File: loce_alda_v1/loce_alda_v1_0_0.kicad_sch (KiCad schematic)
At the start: 82 parts, among them J2 battery_conn_r, J3 track_point_left, J4 niceview_left, J5 niceview_right, J6 track_point_right, SW1 SW_Push, SW10 SW_Push, SW10_r1 SW_Push, SW11 SW_Push, SW11_r1 SW_Push, SW12 SW_Push, SW12_r1 SW_Push, SW13 SW_Push, SW13_r1 SW_Push, SW14 SW_Push, SW14_r1 SW_Push, SW15 SW_Push, SW15_r1 SW_Push, SW16 SW_Push, SW16_r1 SW_Push, SW17 SW_Push, SW17_r1 SW_Push, SW1_r1 SW_Push, SW2 SW_Push, SW2_r1 SW_Push, SW3 SW_Push, SW3_r1 SW_Push, SW4 SW_Push, SW4_r1 SW_Push, SW5 SW_Push, SW5_r1 SW_Push, SW6 SW_Push, SW6_r1 SW_Push, SW7 SW_Push, SW7_r1 SW_Push, SW8 SW_Push, SW8_r1 SW_Push, SW9 SW_Push, SW9_r1 SW_Push, U1 ProMicro-kbd, U2 ProMicro-kbd

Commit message: feat: basic shematics
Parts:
- removed BT1: 1044, 1044:BAT_1044, symbol 1044:1044
- removed Bat+r1, BatGNDr1: MountingHole_Pad, kbd:1pin_conn, symbol Mechanical:MountingHole_Pad
- removed J2: battery_conn_r, Connector_JST:JST_PH_S2B-PH-K_1x02_P2.00mm_Horizontal, symbol Connector:Conn_01x02_Female
- removed U1, U2: ProMicro-kbd, Arduino:Sparkfun_Pro_Micro, symbol Arduino:Sparkfun_Pro_Micro
- added BT1, BT3: Battery, keystone82:batteryHolder_10440_Keystone_82, symbol Device:Battery
- added D35, D36: 1N4148W, Diode_SMD:D_SOD-123, symbol Diode:1N4148W
- added J1, J10, J2, J8: batt_conn, Connector_PinHeader_2.54mm:PinHeader_1x02_P2.54mm_Vertical, symbol Connector:Conn_01x02_Pin
- added J11, J12, J7, J9: batt_conn, Connector_PinSocket_2.54mm:PinSocket_1x02_P2.54mm_Vertical, symbol Connector:Conn_01x02_Socket
- added J13, J14: nfc, Connector_PinSocket_2.54mm:PinSocket_1x02_P2.54mm_Vertical, symbol Connector:Conn_01x02_Socket
- added J15, J16: extra_btn, Connector_PinSocket_2.54mm:PinSocket_1x02_P2.54mm_Vertical, symbol Connector:Conn_01x02_Socket
- added J17: TP_thumb_r, trackpoint:trackpoint_mount_t460s_offset, symbol Connector:Conn_01x01_Pin
- added J18: TP_thumb, trackpoint:trackpoint_mount_t460s_offset, symbol Connector:Conn_01x01_Pin
- added J19: TP_index_r, trackpoint:trackpoint_mount_t460s_offset, symbol Connector:Conn_01x01_Pin
- added J20: TP_index, trackpoint:trackpoint_mount_t460s_offset, symbol Connector:Conn_01x01_Pin
- added U1, U2: SeeeduinoXIAO_BLE, xiao:XIAO-nRF52840-SMD, symbol XIAO:SeeeduinoXIAO_BLE
- added U3, U4: 74HC595, sn74hc595dr:D0016A_N, symbol 74xx:74HC595
- SW1, SW10, SW10_r1, SW11, SW11_r1, SW12, SW12_r1, SW13, SW13_r1, SW14, SW14_r1, SW15, SW15_r1, SW16, SW16_r1, SW17, SW17_r1, SW1_r1, SW2, SW2_r1, SW3, SW3_r1, SW4, SW4_r1, SW5, SW5_r1, SW6, SW6_r1, SW7, SW7_r1, SW8, SW8_r1, SW9, SW9_r1: footprint choc_switch_3d:SW_Hotswap_Kailh_Choc_V1_tweaked -> choc_switch:SW_Hotswap_Kailh_Choc_V1_tweaked_no_clickbar
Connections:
- net ROW3 is gone; now on net ROW2: D16.1 (K), D17.1 (K)
- net ROW3_r is gone; now on net ROW2_r: D33.1 (K), D34.1 (K)
- net BT+: now also BT3.1 (+), J10.1 (Pin_1), J10.2 (Pin_2), J12.1 (Pin_1), J12.2 (Pin_2), J8.1 (Pin_1), J8.2 (Pin_2), J9.1 (Pin_1), J9.2 (Pin_2)
- net BT+_r: now also BT1.1 (+)
- net COL0: now also SW13.1, SW7.1, U4.1 (QB); no longer SW11.1, SW6.1
- net COL0_r: now also SW13_r1.1, SW1_r1.1, SW7_r1.1, U3.1 (QB); no longer SW10_r1.1, SW15_r1.1, SW17_r1.1, SW5_r1.1
- net COL1: now also SW14.1, SW8.1, U4.2 (QC); no longer SW12.1, SW7.1
- net COL1_r: now also SW2_r1.1, SW8_r1.1, U3.2 (QC); no longer SW16_r1.1, SW4_r1.1, SW9_r1.1
- net COL2: now also SW15.1, SW9.1, U4.15 (QA); no longer SW13.1, SW8.1
- net COL2_r: now also SW15_r1.1, SW9_r1.1, U3.15 (QA); no longer SW13_r1.1, SW8_r1.1
- net COL3: now also SW10.1, U4.3 (QD); no longer SW14.1, SW9.1
- net COL3_r: now also SW10_r1.1, SW16_r1.1, SW4_r1.1, U3.3 (QD); no longer SW12_r1.1, SW2_r1.1, SW7_r1.1
- net COL4: now also SW11.1, U4.5 (QF); no longer SW10.1, SW15.1
- net COL4_r: now also SW17_r1.1, SW5_r1.1, U3.5 (QF); no longer SW1_r1.1, SW6_r1.1
- net CS: now also U1.2 (PA4_A1_D1)
- net CS_r: now also U2.2 (PA4_A1_D1)
- net IPD_CLK: now also J3.5 (Pin_5), U1.6 (PA9_A5_D5_SCL)
- net IPD_CLK_r: now also J6.5 (Pin_5), U2.6 (PA9_A5_D5_SCL)
- net IPD_DATA: now also J3.11 (Pin_11), U1.5 (PA8_A4_D4_SDA)
- net IPD_DATA_r: now also J6.11 (Pin_11), U2.5 (PA8_A4_D4_SDA)
- net IPD_RST: now also J3.10 (Pin_10), U1.7 (PB08_A6_D6_TX)
- net IPD_RST_r: now also J6.10 (Pin_10), U2.7 (PB08_A6_D6_TX)
- net MISO: now also U1.11 (PA6_A10_D10_MOSI)
- net MISO_r: now also U2.10 (PA5_A9_D9_MISO)
- net MOSI: now also U1.10 (PA5_A9_D9_MISO), U4.14 (SER)
- net MOSI_r: now also U2.11 (PA6_A10_D10_MOSI), U3.14 (SER)
- net ROW0: now also D6.1 (K), U1.1 (PA02_A0_D0)
- net ROW0_r: now also D23.1 (K), U2.1 (PA02_A0_D0)
- net ROW1: now also D11.1 (K), D12.1 (K), U1.3 (PA10_A2_D2); no longer D6.1 (K)
- net ROW1_r: now also D28.1 (K), D29.1 (K), U2.3 (PA10_A2_D2); no longer D23.1 (K)
- net ROW2: now also D36.1 (K), U1.4 (PA11_A3_D3); no longer D11.1 (K), D12.1 (K)
- net ROW2_r: now also D35.1 (K), U2.4 (PA11_A3_D3); no longer D28.1 (K), D29.1 (K)
- net SCK: now also U1.9 (PA7_A8_D8_SCK), U4.11 (SRCLK)
- net SCK_r: now also U2.9 (PA7_A8_D8_SCK), U3.11 (SRCLK)
- net gnd: now also J3.6 (Pin_6), BT3.2 (-), J1.1 (Pin_1), J1.2 (Pin_2), J11.1 (Pin_1), J11.2 (Pin_2), J2.1 (Pin_1), J2.2 (Pin_2), J7.1 (Pin_1), J7.2 (Pin_2), U1.13 (GND), U4.13 (~{OE}), U4.8 (GND)
- net gnd_r: now also J6.6 (Pin_6), BT1.2 (-), U2.13 (GND), U3.13 (~{OE}), U3.8 (GND)
- net raw: now also U1.16 (BAT+)
- net reset: now also U1.15 (RESET)
- net reset_r: now also U2.15 (RESET)
- net vcc: now also J3.12 (Pin_12), U1.12 (3V3)
- net vcc_r: now also J6.12 (Pin_12), U2.12 (3V3)
- net at D32.2 (A): now also SW15_r1.2; no longer SW11_r1.2
- net at SW16_r1.2: now also D33.2 (A); no longer D34.2 (A)
- net at D23.2 (A): now also SW6_r1.2; no longer SW10_r1.2
- net at SW5_r1.2: now also D22.2 (A); no longer D18.2 (A)
- net at SW7_r1.2: now also D24.2 (A); no longer D26.2 (A)
- net at D19.2 (A): now also SW2_r1.2; no longer SW4_r1.2
- net at D28.2 (A): now also SW11_r1.2; no longer SW15_r1.2
- net at SW12_r1.2: now also D29.2 (A); no longer D31.2 (A)
- net at SW17_r1.2: now also D34.2 (A); no longer D33.2 (A)
- net at SW14_r1.2: now also D31.2 (A); no longer D29.2 (A)
- net at SW1_r1.2: now also D18.2 (A); no longer D22.2 (A)
- net at SW9_r1.2: now also D26.2 (A); no longer D24.2 (A)
- net at D21.2 (A): now also SW4_r1.2; no longer SW2_r1.2
- net at D27.2 (A): now also SW10_r1.2; no longer SW6_r1.2
- new net: D36.2 (A), J15.2 (Pin_2)
- new net: D35.2 (A), J16.2 (Pin_2)
- new net: J13.1 (Pin_1), U1.18 (J13-pin_1)
- new net: J13.2 (Pin_2), U1.17 (J13-pin_2)
- new net: U3.10 (~{SRCLR}), U3.16 (VCC)
- new net: U4.10 (~{SRCLR}), U4.16 (VCC)
- new net COL5: J15.1 (Pin_1), SW12.1, SW6.1, U4.4 (QE)
- new net COL5_r: J16.1 (Pin_1), SW12_r1.1, SW6_r1.1, U3.4 (QE)
- new net SR_CS: U1.8 (PB09_A7_D7_RX), U4.12 (RCLK)
- new net SR_CS_r: U2.8 (PB09_A7_D7_RX), U3.12 (RCLK)
- new net nfc_1_r: J14.1 (Pin_1), U2.18 (J13-pin_1)
- new net nfc_2_r: J14.2 (Pin_2), U2.17 (J13-pin_2)
- new net raw_batt+_r: U2.16 (BAT+)
- no-connect marks 14 -> 12
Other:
- note added: "Shift Register"
- note added: "XIAO BLE"
- note removed: "Nice!Nano"
- company: (none) -> Nathan Bradshaw
- title: (none) -> LOCE ALDA
- moved on the sheet: D1, D10, D11, D12, D13, D14, D15, D16, D17, D18, D19, D2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

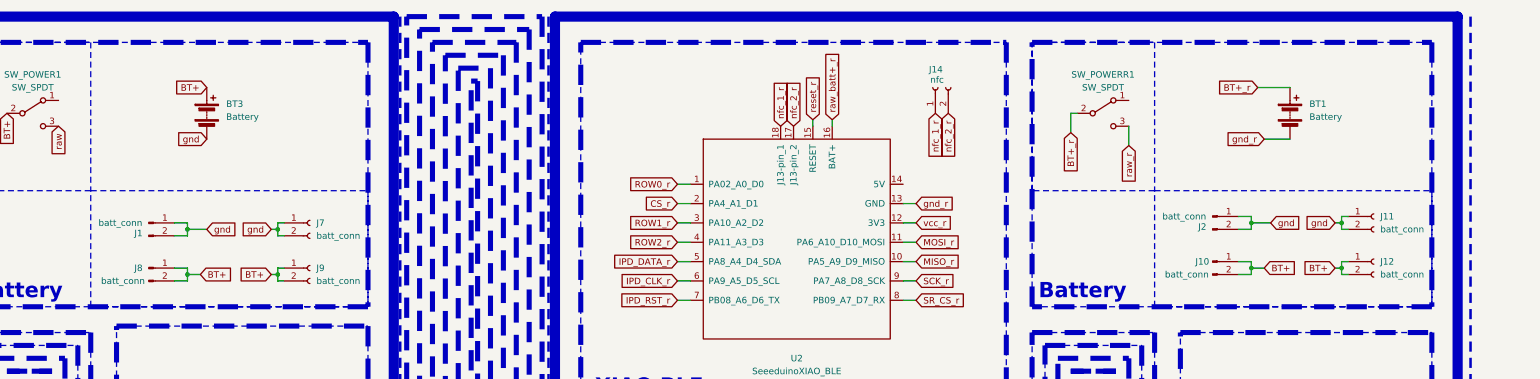
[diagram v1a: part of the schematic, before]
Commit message: feat: more pcb item placements
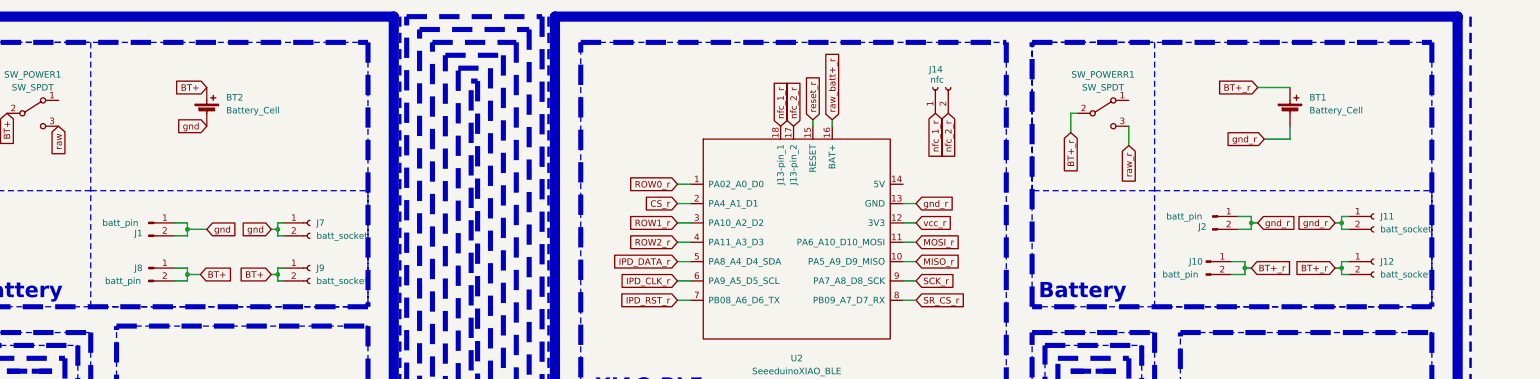
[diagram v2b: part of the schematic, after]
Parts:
- removed BT1, BT3: Battery, keystone82:batteryHolder_10440_Keystone_82, symbol Device:Battery
- added BT1, BT2: Battery_Cell, keystone82:batteryHolder_10440_Keystone_82, symbol Device:Battery_Cell
- J1, J10, J2, J8: value batt_conn -> batt_pin
- J11, J12, J7, J9: value batt_conn -> batt_socket
- RSW1, RSW2: footprint reset_switch:PTS636SP43LFS -> Button_Switch_SMD:Panasonic_EVQPUL_EVQPUC
- SW6, SW6_r1: footprint choc_switch:SW_Hotswap_Kailh_Choc_V1_tweaked_no_clickbar -> choc_switch_3d:SW_Hotswap_Kailh_Choc_V1_tweaked_23du
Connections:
- net BT+: now also BT2.1 (+); no longer J10.1 (Pin_1), J10.2 (Pin_2), J12.1 (Pin_1), J12.2 (Pin_2)
- net BT+_r: now also J10.1 (Pin_1), J10.2 (Pin_2), J12.1 (Pin_1), J12.2 (Pin_2), BT1.1 (+)
- net gnd: now also BT2.2 (-); no longer J11.1 (Pin_1), J11.2 (Pin_2), J2.1 (Pin_1), J2.2 (Pin_2)
- net gnd_r: now also J11.1 (Pin_1), J11.2 (Pin_2), J2.1 (Pin_1), J2.2 (Pin_2), BT1.2 (-)
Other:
- moved on the sheet: J10

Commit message: feat: xiao bottom access
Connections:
- net CS_R is gone; now on net CS_r: J5.5 (Pin_5)
- net raw_batt+_r is gone; now on net BT+_r: U2.16 (BAT+)

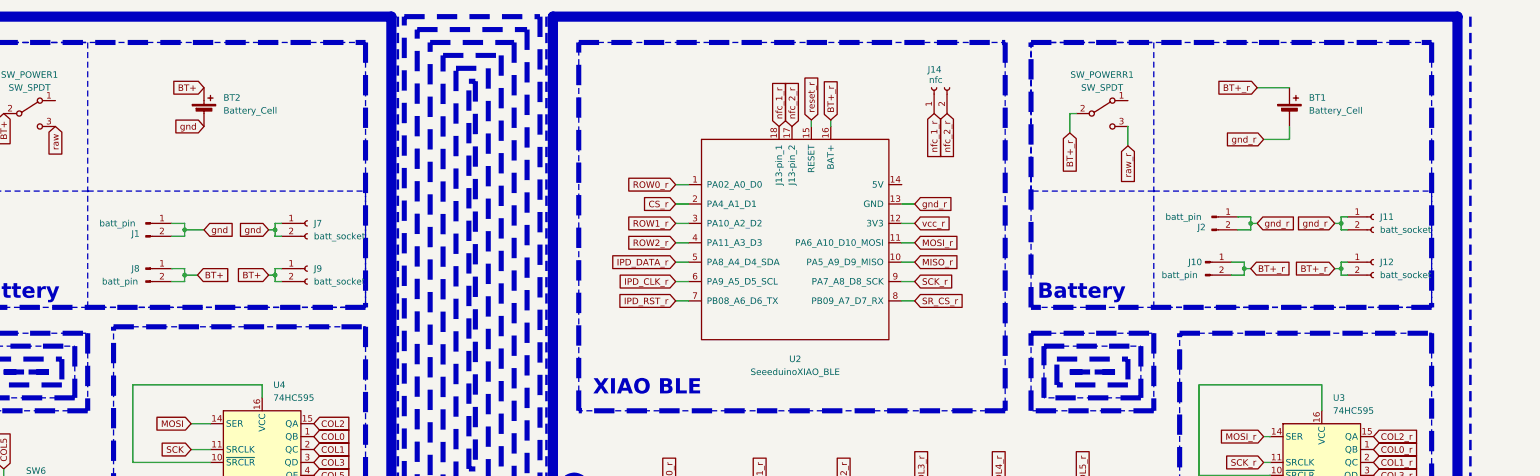
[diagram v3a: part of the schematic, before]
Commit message: feat: remove battery
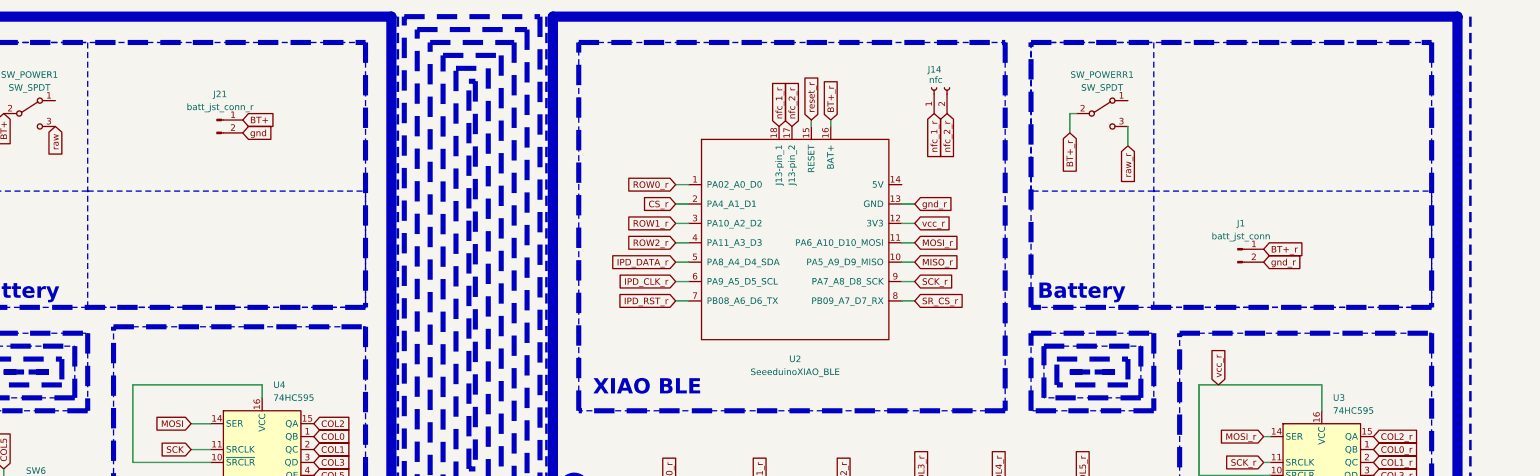
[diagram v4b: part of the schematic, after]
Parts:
- removed BT1, BT2: Battery_Cell, keystone82:batteryHolder_10440_Keystone_82, symbol Device:Battery_Cell
- removed J10, J2, J8: batt_pin, Connector_PinHeader_2.54mm:PinHeader_1x02_P2.54mm_Vertical, symbol Connector:Conn_01x02_Pin
- removed J11, J12, J7, J9: batt_socket, Connector_PinSocket_2.54mm:PinSocket_1x02_P2.54mm_Vertical, symbol Connector:Conn_01x02_Socket
- added J21: batt_jst_conn_r, Connector_JST:JST_PH_S2B-PH-K_1x02_P2.00mm_Horizontal, symbol Connector:Conn_01x02_Pin
- J1: value batt_pin -> batt_jst_conn; footprint Connector_PinHeader_2.54mm:PinHeader_1x02_P2.54mm_Vertical -> Connector_JST:JST_PH_S2B-PH-K_1x02_P2.00mm_Horizontal
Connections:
- net BT+: now also J21.1 (Pin_1)
- net BT+_r: now also J1.1 (Pin_1)
- net gnd: now also J21.2 (Pin_2); no longer J1.1 (Pin_1), J1.2 (Pin_2)
- net gnd_r: now also J1.2 (Pin_2)
- net vcc_r: now also U3.10 (~{SRCLR}), U3.16 (VCC)

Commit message: wip: begin routing
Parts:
- removed J13, J14: nfc, Connector_PinSocket_2.54mm:PinSocket_1x02_P2.54mm_Vertical, symbol Connector:Conn_01x02_Socket
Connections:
- net vcc: now also U4.10 (~{SRCLR}), U4.16 (VCC)
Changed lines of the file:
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@@
 		)
 	)
-	(global_label "nfc_1_r"
-		(shape input)
-		(at 300.99 34.29 270)
-		(fields_autoplaced yes)
-		(effects
-			(font
-				(size 1.27 1.27)
-			)
-			(justify right)
-		)
-		(property "Intersheetrefs" "${INTERSHEET_REFS}"
-			(at 300.99 44.1694 90)
-			(effects
-				(font
-					(size 1.27 1.27)
-				)
-				(justify right)
-				(hide yes)
-			)
-		)
-	)
 	(global_label "SR_CS"
 		(shape input)
@@
 		)
 	)
+	(global_label "vcc"
+		(shape input)
+		(at 143.51 87.63 90)
+		(fields_autoplaced yes)
+		(effects
+			(font
+				(size 1.27 1.27)
+			)
+			(justify left)
+		)
+		(property "Intersheetrefs" "${INTERSHEET_REFS}"
+			(at 143.51 81.5 90)
+			(effects
+				(font
+					(size 1.27 1.27)
+				)
+				(justify left)
+				(hide yes)
+			)
+		)
+	)
 	(global_label "SR_CS"
 		(shape input)
@@
 		)
 	)
-	(global_label "nfc_2_r"
-		(shape input)
-		(at 303.53 34.29 270)
-		(fields_autoplaced yes)
-		(effects
-			(font
-				(size 1.27 1.27)
-			)
-			(justify right)
-		)
-		(property "Intersheetrefs" "${INTERSHEET_REFS}"
-			(at 303.53 44.1694 90)
-			(effects
-				(font
-					(size 1.27 1.27)
-				)
-				(justify right)
-				(hide yes)
-			)
-		)
-	)
 	(global_label "CS_r"
 		(shape input)
@@
 	)
 	(symbol
-		(lib_id "Connector:Conn_01x02_Socket")
-		(at 62.23 31.75 90)
-		(unit 1)
-		(exclude_from_sim no)
-		(in_bom yes)
-		(on_board yes)
-		(dnp no)
-		(property "Reference" "J13"
-			(at 60.96 28.194 90)
-			(effects
-				(font
-					(size 1.27 1.27)
-				)
-				(justify right)
-			)
-		)
-		(property "Value" "nfc"
-			(at 61.214 30.226 90)
-			(effects
-				(font
-					(size 1.27 1.27)
-				)
-				(justify right)
-			)
-		)
-		(property "Footprint" "Connector_PinSocket_2.54mm:PinSocket_1x02_P2.54mm_Vertical"
-			(at 62.23 31.75 0)
-			(effects
-				(font
-					(size 1.27 1.27)
-				)
-				(hide yes)
-			)
-		)
-		(property "Datasheet" "~"
-			(at 62.23 31.75 0)
-			(effects
-				(font
-					(size 1.27 1.27)
-				)
-				(hide yes)
-			)
-		)
-		(property "Description" "Generic connector, single row, 01x02, script generated"
-			(at 62.23 31.75 0)
-			(effects
-				(font
-					(size 1.27 1.27)
-				)
-				(hide yes)
-			)
-		)
-		(pin "2"
-		)
-		(pin "1"
-		)
-		(instances
-			(project "loce_alda_v1_0_0"
-				(path "/38afb63f-a36a-44ef-87ae-e0923e053e07"
-					(reference "J13")
-					(unit 1)
-				)
-			)
-		)
-	)
-	(symbol
 		(lib_id "Switch:SW_Push")
 		(at 304.8 139.7 0)
@@
 					(unit 1)
 				)
-			)
-		)
-	)
-	(symbol
-		(lib_id "Connector:Conn_01x02_Socket")
-		(at 300.99 29.21 90)
-		(unit 1)
-		(exclude_from_sim no)
-		(in_bom yes)
-		(on_board yes)
-		(dnp no)
-		(property "Reference" "J14"
-			(at 299.72 25.654 90)
-			(effects
-				(font
-					(size 1.27 1.27)
-				)
-				(justify right)
-			)
-		)
-		(property "Value" "nfc"
-			(at 299.974 27.686 90)
-			(effects
-				(font
-					(size 1.27 1.27)
-				)
-				(justify right)
-			)
-		)
-		(property "Footprint" "Connector_PinSocket_2.54mm:PinSocket_1x02_P2.54mm_Vertical"
-			(at 300.99 29.21 0)
-			(effects
-				(font
-					(size 1.27 1.27)
-				)
-				(hide yes)
-			)
-		)
-		(property "Datasheet" "~"
-			(at 300.99 29.21 0)
-			(effects
-				(font
-					(size 1.27 1.27)
-				)
-				(hide yes)
-			)
-		)
-		(property "Description" "Generic connector, single row, 01x02, script generated"
-			(at 300.99 29.21 0)
-			(effects
-				(font
-					(size 1.27 1.27)
-				)
-				(hide yes)
-			)
-		)
-		(pin "2"
-		)
-		(pin "1"
-		)
-		(instances
-			(project "loce_alda_v1_0_0"
-				(path "/38afb63f-a36a-44ef-87ae-e0923e053e07"
-					(reference "J14")
-					(unit 1)
-				)
